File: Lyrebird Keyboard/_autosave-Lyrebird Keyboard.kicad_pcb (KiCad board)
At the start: 4 copper layers, 220.1 x 160.3 mm, 99 parts, among them IC1 L7915CV, IC2 L78S15CV, IC3 MCP6022-E_SN, IC4 IR2113SPBF, IC5 IR2113SPBF, IC6 LM358DT, IC7 L7805ACD2T-TR, J1 WAV/ENV 4 (MIDI), J10 AC IN 2, J11 240V Out, J12 240 In, J13 Keys 1 to 14, J14 Keys 15 to 28, J15 Keys 29 to 33, J16 Keys 34 to 45, J17 Keys 46 to 59, J18 Keys 60 to 73, J19 Triangle Test, J2 WAV/ENV 3, J20 AMP Out, J21 SUB Out, J22 Square Test, J23 Bias Test Point 2, J24 Bias Test Point 1, J25 Pedals, J3 WAV/ENV 2, J4 WAV/ENV 1, J5 TONE SRC 4, J6 TONE SRC 3, J7 TONE SRC 2, J8 TONE SRC 1, J9 AC IN 1, Q1 BC848, Q2 BC848, Q3 IRFR2905ZTRPBF, Q4 IRFR2905ZTRPBF, Q5 IRFR2905ZTRPBF, Q6 IRFR2905ZTRPBF, U1 DF06S

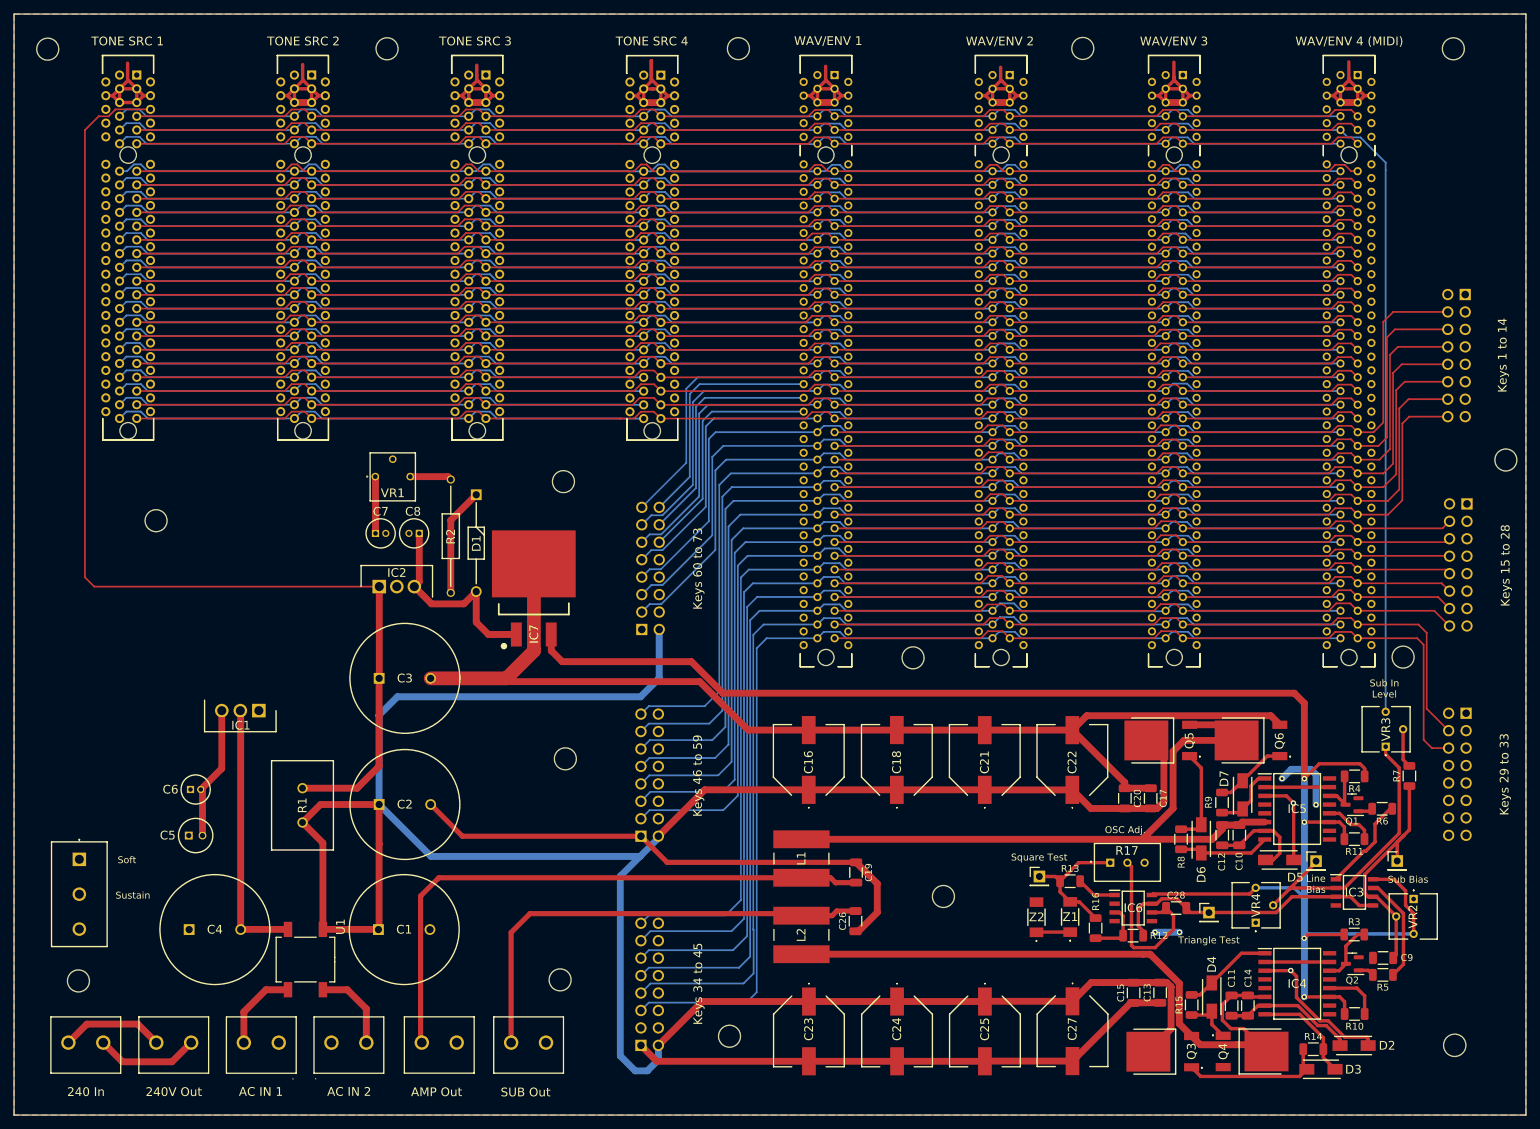
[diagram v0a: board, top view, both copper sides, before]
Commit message: Major Design Changes
Completed Tone Generator Board, board now only provides base notes, individual notes will be generated on the wave shaping boards.

Made major changes to pci slot config, and have increased grounding of the slots.

May need decoupling capacitors on tone generator board, but tight for room
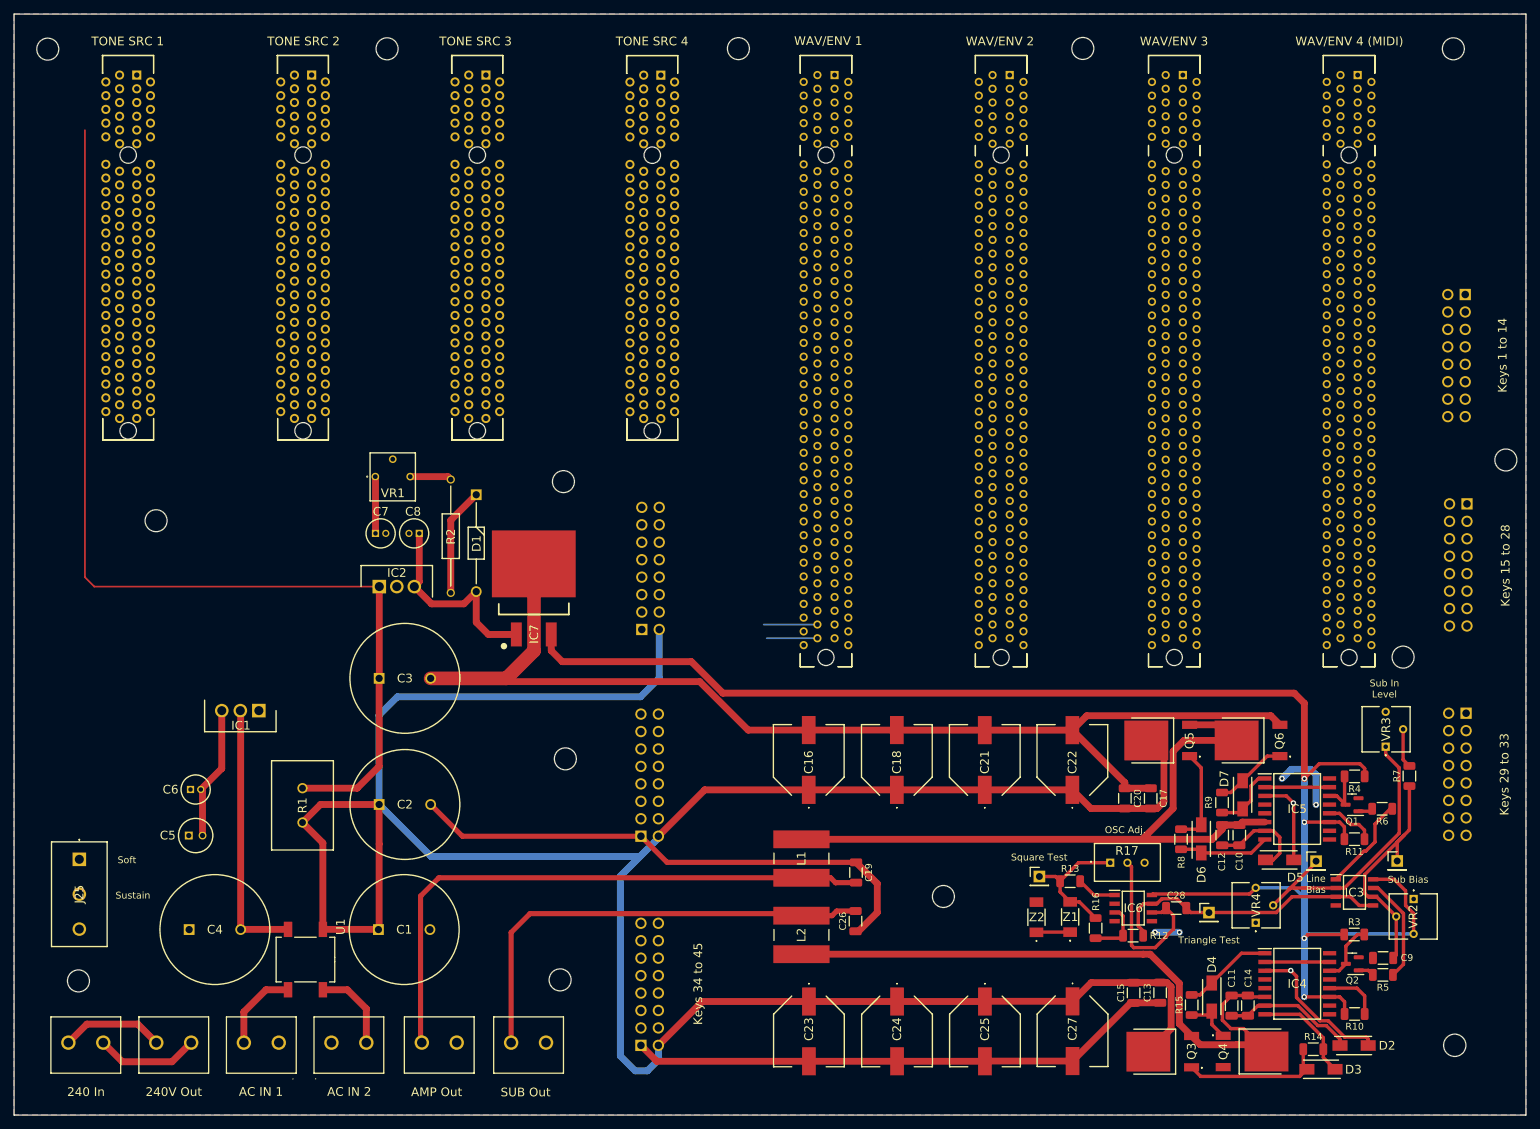
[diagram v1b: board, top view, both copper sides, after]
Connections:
- net A29S renamed EXP 7
- net A5S renamed EXP 6
- net B31S renamed TONE 7
- net B7S renamed TONE 8
- net C#57S renamed TONE 12
- net C32S renamed TONE 10
- net C56S renamed TONE 9
- net C8S renamed TONE 11
- net D#11S renamed EXP 3
- net D#35S renamed EXP 4
- net D#59S renamed EXP 5
- net D10S renamed EXP 12
- net D34S renamed EXP 11
- net E12S renamed TONE 6
- net E36S renamed EXP 1
- net E60S renamed EXP 2
- net EXP4 renamed SELECT 1
- net EXP6 renamed SELECT 2
- net F#38S renamed TONE 1
- net F#62S renamed TONE 2
- net F13S renamed TONE 3
- net F37S renamed TONE 4
- net F61S renamed TONE 5
- net G#40S renamed SELECT 4
- net G#64S renamed SELECT 5
- net G15S renamed SELECT 6
- J1 pad A1: +15V -> GND
- J1 pad A11: G#52S -> GND
- J1 pad A13: G3S -> GND
- J1 pad A15: G27S -> GND
- J1 pad A16: G39S -> +30V
- J1 pad A17: G51S -> GND
- J1 pad A18: G63S -> +15V
- J1 pad A19: F#2S -> GND
- J1 pad A2: -15V -> +30V
- J1 pad A20: F#14S -> -15V
- J1 pad A21: F#26S -> GND
- J1 pad A23: F#50S -> GND
- J1 pad A25: F1S -> GND
- J1 pad A27: F25S -> GND
- J1 pad A29: F49S -> GND
- J1 pad A31: F73S -> GND
- J1 pad A33: E24S -> GND
- J1 pad A35: E48S -> GND
- J1 pad A37: E72S -> GND
- J1 pad A39: D#23S -> GND
- J1 pad A4: GND -> +15V
- J1 pad A41: D#47S -> GND
- J1 pad A43: D#71S -> GND
- J1 pad A45: A17S -> GND
- J1 pad A47: A41S -> F1
- J1 pad A48: A53S -> F#2
- J1 pad A49: A65S -> G3
- J1 pad A50: F1 -> G#4
- J1 pad A51: F#2 -> A5
- J1 pad A52: G3 -> A#6
- J1 pad A53: G#4 -> B7
- J1 pad A54: A5 -> C8
- J1 pad A55: A#6 -> C#9
- J1 pad A56: B7 -> D10
- J1 pad A57: C8 -> D#11
- J1 pad A58: C#9 -> E12
- J1 pad A59: D10 -> F13
- J1 pad A6: +VT -> -15V
- J1 pad A60: D#11 -> F#14
- J1 pad A61: E12 -> G15
- J1 pad A62: F13 -> G#16
- J1 pad A63: F#14 -> A17
- J1 pad A64: G15 -> A#18
- J1 pad A65: G#16 -> B19
- J1 pad A66: A17 -> C20
- J1 pad A67: A#18 -> C#21
- J1 pad A68: B19 -> D22
- J1 pad A69: C20 -> D#23
- J1 pad A7: G#4S -> GND
- J1 pad A70: C#21 -> E24
- J1 pad A71: D22 -> F25
- J1 pad A72: D#23 -> F#26
- J1 pad A73: E24 -> G27
- J1 pad A74: F25 -> G#28
- J1 pad A75: F#26 -> A29
- J1 pad A76: G27 -> A#30
- J1 pad A77: G#28 -> B31
- J1 pad A78: A29 -> C32
- J1 pad A79: A#30 -> C#33
- J1 pad A8: G#16S -> +VT
- J1 pad A80: B31 -> D34
- J1 pad A81: C32 -> D#35
- J1 pad A82: C#33 -> E36
- J1 pad A9: G#28S -> GND
- J1 pad B1: +15V -> GND
- J1 pad B10: EXP8 -> SUSTAIN
- J1 pad B11: EXP9 -> GND
- J1 pad B12: EXP10 -> SOFT
- J1 pad B13: A#66S -> GND
- J1 pad B14: A#54S -> LINE OUT
- J1 pad B15: A#42S -> GND
- J1 pad B16: A#30S -> +30V
- J1 pad B17: A#18S -> GND
- J1 pad B18: A#6S -> +15V
- J1 pad B19: B67S -> GND
- J1 pad B2: -15V -> +30V
- J1 pad B20: B55S -> -15V
- J1 pad B21: B43S -> GND
- J1 pad B23: B19S -> GND
- J1 pad B25: C68S -> GND
- J1 pad B27: C44S -> GND
- J1 pad B29: C20S -> GND
- J1 pad B31: C#69S -> GND
- J1 pad B33: C#45S -> GND
- J1 pad B34: C#33S -> EXP8
- J1 pad B35: C#21S -> GND
- J1 pad B36: C#9S -> EXP9
- J1 pad B37: D70S -> GND
- J1 pad B38: D58S -> EXP10
- J1 pad B39: D46S -> GND
- J1 pad B4: GND -> +15V
- J1 pad B41: D22S -> GND
- J1 pad B43: F73 -> GND
- J1 pad B44: E72 -> EXP 13
- J1 pad B45: D#71 -> GND
- J1 pad B46: D70 -> F73
- J1 pad B47: C#69 -> E72
- J1 pad B48: C68 -> D#71
- J1 pad B49: B67 -> D70
- J1 pad B50: A#66 -> C#69
- J1 pad B51: A65 -> C68
- J1 pad B52: G#64 -> B67
- J1 pad B53: G63 -> A#66
- J1 pad B54: F#62 -> A65
- J1 pad B55: F61 -> G#64
- J1 pad B56: E60 -> G63
- J1 pad B57: D#59 -> F#62
- J1 pad B58: D58 -> F61
- J1 pad B59: C#57 -> E60
- J1 pad B6: +VED -> -15V
- J1 pad B60: C56 -> D#59
- J1 pad B61: B55 -> D58
- J1 pad B62: A#54 -> C#57
- J1 pad B63: A53 -> C56
- J1 pad B64: G#52 -> B55
- J1 pad B65: G51 -> A#54
- J1 pad B66: F#50 -> A53
- J1 pad B67: F49 -> G#52
- J1 pad B68: E48 -> G51
- J1 pad B69: D#47 -> F#50
- J1 pad B7: SUSTAIN -> GND
- J1 pad B70: D46 -> F49
- J1 pad B71: C#45 -> E48
- J1 pad B72: C44 -> D#47
- J1 pad B73: B43 -> D46
- J1 pad B74: A#42 -> C#45
- J1 pad B75: A41 -> C44
- J1 pad B76: G#40 -> B43
- J1 pad B77: G39 -> A#42
- J1 pad B78: F#38 -> A41
- J1 pad B79: F37 -> G#40
- J1 pad B8: SOFT -> +VED
- J1 pad B80: E36 -> G39
- J1 pad B81: D#35 -> F#38
- J1 pad B82: D34 -> F37
- J1 pad B9: LINE OUT -> GND
- J2 pad A1: +15V -> GND
- J2 pad A11: G#52S -> GND
- J2 pad A13: G3S -> GND
- J2 pad A15: G27S -> GND
- J2 pad A16: G39S -> +30V
- J2 pad A17: G51S -> GND
- J2 pad A18: G63S -> +15V
- J2 pad A19: F#2S -> GND
- J2 pad A2: -15V -> +30V
- J2 pad A20: F#14S -> -15V
- J2 pad A21: F#26S -> GND
- J2 pad A23: F#50S -> GND
- J2 pad A25: F1S -> GND
- J2 pad A27: F25S -> GND
- J2 pad A29: F49S -> GND
- J2 pad A31: F73S -> GND
- J2 pad A33: E24S -> GND
- J2 pad A35: E48S -> GND
- J2 pad A37: E72S -> GND
- J2 pad A39: D#23S -> GND
- J2 pad A4: GND -> +15V
- J2 pad A41: D#47S -> GND
- J2 pad A43: D#71S -> GND
- J2 pad A45: A17S -> GND
- J2 pad A47: A41S -> F1
- J2 pad A48: A53S -> F#2
- J2 pad A49: A65S -> G3
- J2 pad A50: F1 -> G#4
- J2 pad A51: F#2 -> A5
- J2 pad A52: G3 -> A#6
- J2 pad A53: G#4 -> B7
- J2 pad A54: A5 -> C8
- J2 pad A55: A#6 -> C#9
- J2 pad A56: B7 -> D10
- J2 pad A57: C8 -> D#11
- J2 pad A58: C#9 -> E12
- J2 pad A59: D10 -> F13
- J2 pad A6: +VT -> -15V
- J2 pad A60: D#11 -> F#14
- J2 pad A61: E12 -> G15
- J2 pad A62: F13 -> G#16
- J2 pad A63: F#14 -> A17
- J2 pad A64: G15 -> A#18
- J2 pad A65: G#16 -> B19
- J2 pad A66: A17 -> C20
- J2 pad A67: A#18 -> C#21
- J2 pad A68: B19 -> D22
- J2 pad A69: C20 -> D#23
- J2 pad A7: G#4S -> GND
- J2 pad A70: C#21 -> E24
- J2 pad A71: D22 -> F25
- J2 pad A72: D#23 -> F#26
- J2 pad A73: E24 -> G27
- J2 pad A74: F25 -> G#28
- J2 pad A75: F#26 -> A29
- J2 pad A76: G27 -> A#30
- J2 pad A77: G#28 -> B31
- J2 pad A78: A29 -> C32
- J2 pad A79: A#30 -> C#33
- J2 pad A8: G#16S -> +VT
- J2 pad A80: B31 -> D34
- J2 pad A81: C32 -> D#35
- J2 pad A82: C#33 -> E36
- J2 pad A9: G#28S -> GND
- J2 pad B1: +15V -> GND
- J2 pad B10: EXP8 -> SUSTAIN
- J2 pad B11: EXP9 -> GND
- J2 pad B12: EXP10 -> SOFT
- J2 pad B13: A#66S -> GND
- J2 pad B14: A#54S -> LINE OUT
- J2 pad B15: A#42S -> GND
- J2 pad B16: A#30S -> +30V
- J2 pad B17: A#18S -> GND
- J2 pad B18: A#6S -> +15V
- J2 pad B19: B67S -> GND
- J2 pad B2: -15V -> +30V
- J2 pad B20: B55S -> -15V
- J2 pad B21: B43S -> GND
- J2 pad B23: B19S -> GND
- J2 pad B25: C68S -> GND
- J2 pad B27: C44S -> GND
- J2 pad B29: C20S -> GND
- J2 pad B31: C#69S -> GND
- J2 pad B33: C#45S -> GND
- J2 pad B34: C#33S -> EXP8
- J2 pad B35: C#21S -> GND
- J2 pad B36: C#9S -> EXP9
- J2 pad B37: D70S -> GND
- J2 pad B38: D58S -> EXP10
- J2 pad B39: D46S -> GND
- J2 pad B4: GND -> +15V
- J2 pad B41: D22S -> GND
- J2 pad B43: F73 -> GND
- J2 pad B44: E72 -> EXP 13
- J2 pad B45: D#71 -> GND
- J2 pad B46: D70 -> F73
- J2 pad B47: C#69 -> E72
- J2 pad B48: C68 -> D#71
- J2 pad B49: B67 -> D70
- J2 pad B50: A#66 -> C#69
- J2 pad B51: A65 -> C68
- J2 pad B52: G#64 -> B67
- J2 pad B53: G63 -> A#66
- J2 pad B54: F#62 -> A65
- J2 pad B55: F61 -> G#64
- J2 pad B56: E60 -> G63
- J2 pad B57: D#59 -> F#62
- J2 pad B58: D58 -> F61
- J2 pad B59: C#57 -> E60
- J2 pad B6: +VED -> -15V
- J2 pad B60: C56 -> D#59
- J2 pad B61: B55 -> D58
- J2 pad B62: A#54 -> C#57
- J2 pad B63: A53 -> C56
- J2 pad B64: G#52 -> B55
- J2 pad B65: G51 -> A#54
- J2 pad B66: F#50 -> A53
- J2 pad B67: F49 -> G#52
- J2 pad B68: E48 -> G51
- J2 pad B69: D#47 -> F#50
- J2 pad B7: SUSTAIN -> GND
- J2 pad B70: D46 -> F49
- J2 pad B71: C#45 -> E48
- J2 pad B72: C44 -> D#47
- J2 pad B73: B43 -> D46
- J2 pad B74: A#42 -> C#45
- J2 pad B75: A41 -> C44
- J2 pad B76: G#40 -> B43
- J2 pad B77: G39 -> A#42
- J2 pad B78: F#38 -> A41
- J2 pad B79: F37 -> G#40
- J2 pad B8: SOFT -> +VED
- J2 pad B80: E36 -> G39
- J2 pad B81: D#35 -> F#38
- J2 pad B82: D34 -> F37
- J2 pad B9: LINE OUT -> GND
- J3 pad A1: +15V -> GND
- J3 pad A11: G#52S -> GND
- J3 pad A13: G3S -> GND
- J3 pad A15: G27S -> GND
- J3 pad A16: G39S -> +30V
- J3 pad A17: G51S -> GND
- J3 pad A18: G63S -> +15V
- J3 pad A19: F#2S -> GND
- J3 pad A2: -15V -> +30V
- J3 pad A20: F#14S -> -15V
- J3 pad A21: F#26S -> GND
- J3 pad A23: F#50S -> GND
- J3 pad A25: F1S -> GND
- J3 pad A27: F25S -> GND
- J3 pad A29: F49S -> GND
- J3 pad A31: F73S -> GND
- J3 pad A33: E24S -> GND
- J3 pad A35: E48S -> GND
- J3 pad A37: E72S -> GND
- J3 pad A39: D#23S -> GND
- J3 pad A4: GND -> +15V
- J3 pad A41: D#47S -> GND
- J3 pad A43: D#71S -> GND
- J3 pad A45: A17S -> GND
- J3 pad A47: A41S -> F1
- J3 pad A48: A53S -> F#2
- J3 pad A49: A65S -> G3
- J3 pad A50: F1 -> G#4
- J3 pad A51: F#2 -> A5
- J3 pad A52: G3 -> A#6
- J3 pad A53: G#4 -> B7
- J3 pad A54: A5 -> C8
- J3 pad A55: A#6 -> C#9
- J3 pad A56: B7 -> D10
- J3 pad A57: C8 -> D#11
- J3 pad A58: C#9 -> E12
- J3 pad A59: D10 -> F13
- J3 pad A6: +VT -> -15V
- J3 pad A60: D#11 -> F#14
- J3 pad A61: E12 -> G15
- J3 pad A62: F13 -> G#16
- J3 pad A63: F#14 -> A17
- J3 pad A64: G15 -> A#18
- J3 pad A65: G#16 -> B19
- J3 pad A66: A17 -> C20
- J3 pad A67: A#18 -> C#21
- J3 pad A68: B19 -> D22
- J3 pad A69: C20 -> D#23
- J3 pad A7: G#4S -> GND
- J3 pad A70: C#21 -> E24
- J3 pad A71: D22 -> F25
- J3 pad A72: D#23 -> F#26
- J3 pad A73: E24 -> G27
- J3 pad A74: F25 -> G#28
- J3 pad A75: F#26 -> A29
- J3 pad A76: G27 -> A#30
- J3 pad A77: G#28 -> B31
- J3 pad A78: A29 -> C32
- J3 pad A79: A#30 -> C#33
- J3 pad A8: G#16S -> +VT
- J3 pad A80: B31 -> D34
- J3 pad A81: C32 -> D#35
- J3 pad A82: C#33 -> E36
- J3 pad A9: G#28S -> GND
- J3 pad B1: +15V -> GND
- J3 pad B10: EXP8 -> SUSTAIN
- J3 pad B11: EXP9 -> GND
- J3 pad B12: EXP10 -> SOFT
- J3 pad B13: A#66S -> GND
- J3 pad B14: A#54S -> LINE OUT
- J3 pad B15: A#42S -> GND
- J3 pad B16: A#30S -> +30V
- J3 pad B17: A#18S -> GND
- J3 pad B18: A#6S -> +15V
- J3 pad B19: B67S -> GND
- J3 pad B2: -15V -> +30V
- J3 pad B20: B55S -> -15V
- J3 pad B21: B43S -> GND
- J3 pad B23: B19S -> GND
- J3 pad B25: C68S -> GND
- J3 pad B27: C44S -> GND
- J3 pad B29: C20S -> GND
- J3 pad B31: C#69S -> GND
- J3 pad B33: C#45S -> GND
- J3 pad B34: C#33S -> EXP8
- J3 pad B35: C#21S -> GND
- J3 pad B36: C#9S -> EXP9
- J3 pad B37: D70S -> GND
- J3 pad B38: D58S -> EXP10
- J3 pad B39: D46S -> GND
- J3 pad B4: GND -> +15V
- J3 pad B41: D22S -> GND
- J3 pad B43: F73 -> GND
- J3 pad B44: E72 -> EXP 13
- J3 pad B45: D#71 -> GND
- J3 pad B46: D70 -> F73
- J3 pad B47: C#69 -> E72
- J3 pad B48: C68 -> D#71
- J3 pad B49: B67 -> D70
- J3 pad B50: A#66 -> C#69
- J3 pad B51: A65 -> C68
- J3 pad B52: G#64 -> B67
- J3 pad B53: G63 -> A#66
- J3 pad B54: F#62 -> A65
- J3 pad B55: F61 -> G#64
- J3 pad B56: E60 -> G63
- J3 pad B57: D#59 -> F#62
- J3 pad B58: D58 -> F61
- J3 pad B59: C#57 -> E60
- J3 pad B6: +VED -> -15V
- J3 pad B60: C56 -> D#59
- J3 pad B61: B55 -> D58
- J3 pad B62: A#54 -> C#57
- J3 pad B63: A53 -> C56
- J3 pad B64: G#52 -> B55
- J3 pad B65: G51 -> A#54
- J3 pad B66: F#50 -> A53
- J3 pad B67: F49 -> G#52
- J3 pad B68: E48 -> G51
- J3 pad B69: D#47 -> F#50
- J3 pad B7: SUSTAIN -> GND
- J3 pad B70: D46 -> F49
- J3 pad B71: C#45 -> E48
- J3 pad B72: C44 -> D#47
- J3 pad B73: B43 -> D46
- J3 pad B74: A#42 -> C#45
- J3 pad B75: A41 -> C44
- J3 pad B76: G#40 -> B43
- J3 pad B77: G39 -> A#42
- J3 pad B78: F#38 -> A41
- J3 pad B79: F37 -> G#40
- J3 pad B8: SOFT -> +VED
- J3 pad B80: E36 -> G39
- J3 pad B81: D#35 -> F#38
- J3 pad B82: D34 -> F37
- J3 pad B9: LINE OUT -> GND
- J4 pad A1: +15V -> GND
- J4 pad A11: G#52S -> GND
- J4 pad A13: G3S -> GND
- J4 pad A15: G27S -> GND
- J4 pad A16: G39S -> +30V
- J4 pad A17: G51S -> GND
- J4 pad A18: G63S -> +15V
- J4 pad A19: F#2S -> GND
- J4 pad A2: -15V -> +30V
- J4 pad A20: F#14S -> -15V
- J4 pad A21: F#26S -> GND
- J4 pad A23: F#50S -> GND
- J4 pad A25: F1S -> GND
- J4 pad A27: F25S -> GND
- J4 pad A29: F49S -> GND
- J4 pad A31: F73S -> GND
- J4 pad A33: E24S -> GND
- J4 pad A35: E48S -> GND
- J4 pad A37: E72S -> GND
- J4 pad A39: D#23S -> GND
- J4 pad A4: GND -> +15V
- J4 pad A41: D#47S -> GND
- J4 pad A43: D#71S -> GND
- J4 pad A45: A17S -> GND
- J4 pad A47: A41S -> F1
- J4 pad A48: A53S -> F#2
- J4 pad A49: A65S -> G3
- J4 pad A50: F1 -> G#4
- J4 pad A51: F#2 -> A5
- J4 pad A52: G3 -> A#6
- J4 pad A53: G#4 -> B7
- J4 pad A54: A5 -> C8
- J4 pad A55: A#6 -> C#9
- J4 pad A56: B7 -> D10
- J4 pad A57: C8 -> D#11
- J4 pad A58: C#9 -> E12
- J4 pad A59: D10 -> F13
- J4 pad A6: +VT -> -15V
- J4 pad A60: D#11 -> F#14
- J4 pad A61: E12 -> G15
- J4 pad A62: F13 -> G#16
- J4 pad A63: F#14 -> A17
- J4 pad A64: G15 -> A#18
- J4 pad A65: G#16 -> B19
- J4 pad A66: A17 -> C20
- J4 pad A67: A#18 -> C#21
- J4 pad A68: B19 -> D22
- J4 pad A69: C20 -> D#23
- J4 pad A7: G#4S -> GND
- J4 pad A70: C#21 -> E24
- J4 pad A71: D22 -> F25
- J4 pad A72: D#23 -> F#26
- J4 pad A73: E24 -> G27
- J4 pad A74: F25 -> G#28
- J4 pad A75: F#26 -> A29
- J4 pad A76: G27 -> A#30
- J4 pad A77: G#28 -> B31
- J4 pad A78: A29 -> C32
- J4 pad A79: A#30 -> C#33
- J4 pad A8: G#16S -> +VT
- J4 pad A80: B31 -> D34
- J4 pad A81: C32 -> D#35
- J4 pad A82: C#33 -> E36
- J4 pad A9: G#28S -> GND
- J4 pad B1: +15V -> GND
- J4 pad B10: EXP8 -> SUSTAIN
- J4 pad B11: EXP9 -> GND
- J4 pad B12: EXP10 -> SOFT
- J4 pad B13: A#66S -> GND
- J4 pad B14: A#54S -> LINE OUT
- J4 pad B15: A#42S -> GND
- J4 pad B16: A#30S -> +30V
- J4 pad B17: A#18S -> GND
- J4 pad B18: A#6S -> +15V
- J4 pad B19: B67S -> GND
- J4 pad B2: -15V -> +30V
- J4 pad B20: B55S -> -15V
- J4 pad B21: B43S -> GND
- J4 pad B23: B19S -> GND
- J4 pad B25: C68S -> GND
- J4 pad B27: C44S -> GND
- J4 pad B29: C20S -> GND
- J4 pad B31: C#69S -> GND
- J4 pad B33: C#45S -> GND
- J4 pad B34: C#33S -> EXP8
- J4 pad B35: C#21S -> GND
- J4 pad B36: C#9S -> EXP9
- J4 pad B37: D70S -> GND
- J4 pad B38: D58S -> EXP10
- J4 pad B39: D46S -> GND
- J4 pad B4: GND -> +15V
- J4 pad B41: D22S -> GND
- J4 pad B43: F73 -> GND
- J4 pad B44: E72 -> EXP 13
- J4 pad B45: D#71 -> GND
- J4 pad B46: D70 -> F73
- J4 pad B47: C#69 -> E72
- J4 pad B48: C68 -> D#71
- J4 pad B49: B67 -> D70
- J4 pad B50: A#66 -> C#69
- J4 pad B51: A65 -> C68
- J4 pad B52: G#64 -> B67
- J4 pad B53: G63 -> A#66
- J4 pad B54: F#62 -> A65
- J4 pad B55: F61 -> G#64
- J4 pad B56: E60 -> G63
- J4 pad B57: D#59 -> F#62
- J4 pad B58: D58 -> F61
- J4 pad B59: C#57 -> E60
- J4 pad B6: +VED -> -15V
- J4 pad B60: C56 -> D#59
- J4 pad B61: B55 -> D58
- J4 pad B62: A#54 -> C#57
- J4 pad B63: A53 -> C56
- J4 pad B64: G#52 -> B55
- J4 pad B65: G51 -> A#54
- J4 pad B66: F#50 -> A53
- J4 pad B67: F49 -> G#52
- J4 pad B68: E48 -> G51
- J4 pad B69: D#47 -> F#50
- J4 pad B7: SUSTAIN -> GND
- J4 pad B70: D46 -> F49
- J4 pad B71: C#45 -> E48
- J4 pad B72: C44 -> D#47
- J4 pad B73: B43 -> D46
- J4 pad B74: A#42 -> C#45
- J4 pad B75: A41 -> C44
- J4 pad B76: G#40 -> B43
- J4 pad B77: G39 -> A#42
- J4 pad B78: F#38 -> A41
- J4 pad B79: F37 -> G#40
- J4 pad B8: SOFT -> +VED
- J4 pad B80: E36 -> G39
- J4 pad B81: D#35 -> F#38
- J4 pad B82: D34 -> F37
- J4 pad B9: LINE OUT -> GND
- J5 pad A1: +15V -> GND
- J5 pad A11: G#52S -> GND
- J5 pad A13: G3S -> GND
- J5 pad A15: G27S -> GND
- J5 pad A16: G39S -> +30V
- J5 pad A17: G51S -> GND
- J5 pad A18: G63S -> +15V
- J5 pad A19: F#2S -> GND
- J5 pad A2: -15V -> +30V
- J5 pad A20: F#14S -> -15V
- J5 pad A21: F#26S -> GND
- J5 pad A23: F#50S -> GND
- J5 pad A25: F1S -> GND
- J5 pad A27: F25S -> GND
- J5 pad A29: F49S -> GND
- J5 pad A31: F73S -> GND
- J5 pad A33: E24S -> GND
- J5 pad A35: E48S -> GND
- J5 pad A37: E72S -> GND
- J5 pad A39: D#23S -> GND
- J5 pad A4: GND -> +15V
- J5 pad A41: D#47S -> GND
- J5 pad A43: D#71S -> GND
- J5 pad A45: A17S -> GND
- J5 pad A47: A41S -> GND
- J5 pad A48: A53S -> SELECT 3
- J5 pad A49: A65S -> GND
- J5 pad A6: +VT -> -15V
- J5 pad A7: G#4S -> GND
- J5 pad A8: G#16S -> +VT
- J5 pad A9: G#28S -> GND
- J5 pad B1: +15V -> GND
- J5 pad B10: EXP8 -> SUSTAIN
- J5 pad B11: EXP9 -> GND
- J5 pad B12: EXP10 -> SOFT
- J5 pad B13: A#66S -> GND
- J5 pad B14: A#54S -> LINE OUT
- J5 pad B15: A#42S -> GND
- J5 pad B16: A#30S -> +30V
- J5 pad B17: A#18S -> GND
- J5 pad B18: A#6S -> +15V
- J5 pad B19: B67S -> GND
- J5 pad B2: -15V -> +30V
- J5 pad B20: B55S -> -15V
- J5 pad B21: B43S -> GND
- J5 pad B23: B19S -> GND
- J5 pad B25: C68S -> GND
- J5 pad B27: C44S -> GND
- J5 pad B29: C20S -> GND
- J5 pad B31: C#69S -> GND
- J5 pad B33: C#45S -> GND
- J5 pad B34: C#33S -> EXP8
- J5 pad B35: C#21S -> GND
- J5 pad B36: C#9S -> EXP9
- J5 pad B37: D70S -> GND
- J5 pad B38: D58S -> EXP10
- J5 pad B39: D46S -> GND
- J5 pad B4: GND -> +15V
- J5 pad B41: D22S -> GND
- J5 pad B43: EXP1 -> GND
- J5 pad B44: EXP2 -> EXP 13
- J5 pad B45: EXP3 -> GND
- J5 pad B47: EXP5 -> GND
- J5 pad B49: EXP7 -> GND
- J5 pad B6: +VED -> -15V
- J5 pad B7: SUSTAIN -> GND
- J5 pad B8: SOFT -> +VED
- J5 pad B9: LINE OUT -> GND
- J6 pad A1: +15V -> GND
- J6 pad A11: G#52S -> GND
- J6 pad A13: G3S -> GND
- J6 pad A15: G27S -> GND
- J6 pad A16: G39S -> +30V
- J6 pad A17: G51S -> GND
- J6 pad A18: G63S -> +15V
- J6 pad A19: F#2S -> GND
- J6 pad A2: -15V -> +30V
- J6 pad A20: F#14S -> -15V
- J6 pad A21: F#26S -> GND
- J6 pad A23: F#50S -> GND
- J6 pad A25: F1S -> GND
- J6 pad A27: F25S -> GND
- J6 pad A29: F49S -> GND
- J6 pad A31: F73S -> GND
- J6 pad A33: E24S -> GND
- J6 pad A35: E48S -> GND
- J6 pad A37: E72S -> GND
- J6 pad A39: D#23S -> GND
- J6 pad A4: GND -> +15V
- J6 pad A41: D#47S -> GND
- J6 pad A43: D#71S -> GND
- J6 pad A45: A17S -> GND
- J6 pad A47: A41S -> GND
- J6 pad A48: A53S -> SELECT 3
- J6 pad A49: A65S -> GND
- J6 pad A6: +VT -> -15V
- J6 pad A7: G#4S -> GND
- J6 pad A8: G#16S -> +VT
- J6 pad A9: G#28S -> GND
- J6 pad B1: +15V -> GND
- J6 pad B10: EXP8 -> SUSTAIN
- J6 pad B11: EXP9 -> GND
- J6 pad B12: EXP10 -> SOFT
- J6 pad B13: A#66S -> GND
- J6 pad B14: A#54S -> LINE OUT
- J6 pad B15: A#42S -> GND
- J6 pad B16: A#30S -> +30V
- J6 pad B17: A#18S -> GND
- J6 pad B18: A#6S -> +15V
- J6 pad B19: B67S -> GND
- J6 pad B2: -15V -> +30V
- J6 pad B20: B55S -> -15V
- J6 pad B21: B43S -> GND
- J6 pad B23: B19S -> GND
- J6 pad B25: C68S -> GND
- J6 pad B27: C44S -> GND
- J6 pad B29: C20S -> GND
- J6 pad B31: C#69S -> GND
- J6 pad B33: C#45S -> GND
- J6 pad B34: C#33S -> EXP8
- J6 pad B35: C#21S -> GND
- J6 pad B36: C#9S -> EXP9
- J6 pad B37: D70S -> GND
- J6 pad B38: D58S -> EXP10
- J6 pad B39: D46S -> GND
- J6 pad B4: GND -> +15V
- J6 pad B41: D22S -> GND
- J6 pad B43: EXP1 -> GND
- J6 pad B44: EXP2 -> EXP 13
- J6 pad B45: EXP3 -> GND
- J6 pad B47: EXP5 -> GND
- J6 pad B49: EXP7 -> GND
- J6 pad B6: +VED -> -15V
- J6 pad B7: SUSTAIN -> GND
- J6 pad B8: SOFT -> +VED
- J6 pad B9: LINE OUT -> GND
- J7 pad A1: +15V -> GND
- J7 pad A11: G#52S -> GND
- J7 pad A13: G3S -> GND
- J7 pad A15: G27S -> GND
- J7 pad A16: G39S -> +30V
- J7 pad A17: G51S -> GND
- J7 pad A18: G63S -> +15V
- J7 pad A19: F#2S -> GND
- J7 pad A2: -15V -> +30V
- J7 pad A20: F#14S -> -15V
- J7 pad A21: F#26S -> GND
- J7 pad A23: F#50S -> GND
- J7 pad A25: F1S -> GND
- J7 pad A27: F25S -> GND
- J7 pad A29: F49S -> GND
- J7 pad A31: F73S -> GND
- J7 pad A33: E24S -> GND
- J7 pad A35: E48S -> GND
- J7 pad A37: E72S -> GND
- J7 pad A39: D#23S -> GND
- J7 pad A4: GND -> +15V
- J7 pad A41: D#47S -> GND
- J7 pad A43: D#71S -> GND
- J7 pad A45: A17S -> GND
- J7 pad A47: A41S -> GND
- J7 pad A48: A53S -> SELECT 3
- J7 pad A49: A65S -> GND
- J7 pad A6: +VT -> -15V
- J7 pad A7: G#4S -> GND
- J7 pad A8: G#16S -> +VT
- J7 pad A9: G#28S -> GND
- J7 pad B1: +15V -> GND
- J7 pad B10: EXP8 -> SUSTAIN
- J7 pad B11: EXP9 -> GND
- J7 pad B12: EXP10 -> SOFT
- J7 pad B13: A#66S -> GND
- J7 pad B14: A#54S -> LINE OUT
- J7 pad B15: A#42S -> GND
- J7 pad B16: A#30S -> +30V
- J7 pad B17: A#18S -> GND
- J7 pad B18: A#6S -> +15V
- J7 pad B19: B67S -> GND
- J7 pad B2: -15V -> +30V
- J7 pad B20: B55S -> -15V
- J7 pad B21: B43S -> GND
- J7 pad B23: B19S -> GND
- J7 pad B25: C68S -> GND
- J7 pad B27: C44S -> GND
- J7 pad B29: C20S -> GND
- J7 pad B31: C#69S -> GND
- J7 pad B33: C#45S -> GND
- J7 pad B34: C#33S -> EXP8
- J7 pad B35: C#21S -> GND
- J7 pad B36: C#9S -> EXP9
- J7 pad B37: D70S -> GND
- J7 pad B38: D58S -> EXP10
- J7 pad B39: D46S -> GND
- J7 pad B4: GND -> +15V
- J7 pad B41: D22S -> GND
- J7 pad B43: EXP1 -> GND
- J7 pad B44: EXP2 -> EXP 13
- J7 pad B45: EXP3 -> GND
- J7 pad B47: EXP5 -> GND
- J7 pad B49: EXP7 -> GND
- J7 pad B6: +VED -> -15V
- J7 pad B7: SUSTAIN -> GND
- J7 pad B8: SOFT -> +VED
- J7 pad B9: LINE OUT -> GND
- J8 pad A1: +15V -> GND
- J8 pad A11: G#52S -> GND
- J8 pad A13: G3S -> GND
- J8 pad A15: G27S -> GND
- J8 pad A16: G39S -> +30V
- J8 pad A17: G51S -> GND
- J8 pad A18: G63S -> +15V
- J8 pad A19: F#2S -> GND
- J8 pad A2: -15V -> +30V
- J8 pad A20: F#14S -> -15V
- J8 pad A21: F#26S -> GND
- J8 pad A23: F#50S -> GND
- J8 pad A25: F1S -> GND
- J8 pad A27: F25S -> GND
- J8 pad A29: F49S -> GND
- J8 pad A31: F73S -> GND
- J8 pad A33: E24S -> GND
- J8 pad A35: E48S -> GND
- J8 pad A37: E72S -> GND
- J8 pad A39: D#23S -> GND
- J8 pad A4: GND -> +15V
- J8 pad A41: D#47S -> GND
- J8 pad A43: D#71S -> GND
- J8 pad A45: A17S -> GND
- J8 pad A47: A41S -> GND
- J8 pad A48: A53S -> SELECT 3
- J8 pad A49: A65S -> GND
- J8 pad A6: +VT -> -15V
- J8 pad A7: G#4S -> GND
- J8 pad A8: G#16S -> +VT
- J8 pad A9: G#28S -> GND
- J8 pad B1: +15V -> GND
- J8 pad B10: EXP8 -> SUSTAIN
- J8 pad B11: EXP9 -> GND
- J8 pad B12: EXP10 -> SOFT
- J8 pad B13: A#66S -> GND
- J8 pad B14: A#54S -> LINE OUT
- J8 pad B15: A#42S -> GND
- J8 pad B16: A#30S -> +30V
- J8 pad B17: A#18S -> GND
- J8 pad B18: A#6S -> +15V
- J8 pad B19: B67S -> GND
- J8 pad B2: -15V -> +30V
- J8 pad B20: B55S -> -15V
- J8 pad B21: B43S -> GND
- J8 pad B23: B19S -> GND
- J8 pad B25: C68S -> GND
- J8 pad B27: C44S -> GND
- J8 pad B29: C20S -> GND
- J8 pad B31: C#69S -> GND
- J8 pad B33: C#45S -> GND
- J8 pad B34: C#33S -> EXP8
- J8 pad B35: C#21S -> GND
- J8 pad B36: C#9S -> EXP9
- J8 pad B37: D70S -> GND
- J8 pad B38: D58S -> EXP10
- J8 pad B39: D46S -> GND
- J8 pad B4: GND -> +15V
- J8 pad B41: D22S -> GND
- J8 pad B43: EXP1 -> GND
- J8 pad B44: EXP2 -> EXP 13
- J8 pad B45: EXP3 -> GND
- J8 pad B47: EXP5 -> GND
- J8 pad B49: EXP7 -> GND
- J8 pad B6: +VED -> -15V
- J8 pad B7: SUSTAIN -> GND
- J8 pad B8: SOFT -> +VED
- J8 pad B9: LINE OUT -> GND
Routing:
- net SUSTAIN: track 305.7 -> 0.00 mm
- net SOFT: track 297.4 -> 0.00 mm
- net +VED: track 279.4 -> 0.00 mm
- net LINE OUT: track 271.9 -> 0.00 mm
- net A53S: track 204.3 -> 0.00 mm
- net +VT: track 342.3 -> 147.2 mm
- net EXP 6: track 191.4 -> 0.00 mm
- net TONE 4: track 191.3 -> 0.00 mm
- net EXP 1: track 191.3 -> 0.00 mm
- net SELECT 5: track 191.2 -> 0.00 mm
- net TONE 3: track 191.1 -> 0.00 mm
- net TONE 5: track 191.1 -> 0.00 mm
- net F#14S: track 191.1 -> 0.00 mm
- net EXP 4: track 191.1 -> 0.00 mm
- net TONE 1: track 191.1 -> 0.00 mm
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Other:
- outline, holes or cut-outs redrawn
